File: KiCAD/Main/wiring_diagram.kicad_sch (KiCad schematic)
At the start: 19 parts, among them J5 Screw_Terminal_01x09, J6 Screw_Terminal_01x09, M1 Motor_Servo [Axon Mini MkII], M2 Motor_Servo [Axon Mini MkII], SW3 Screw Switch, SW4 Screw Switch, SW5 Screw Switch, SW6 Screw Switch

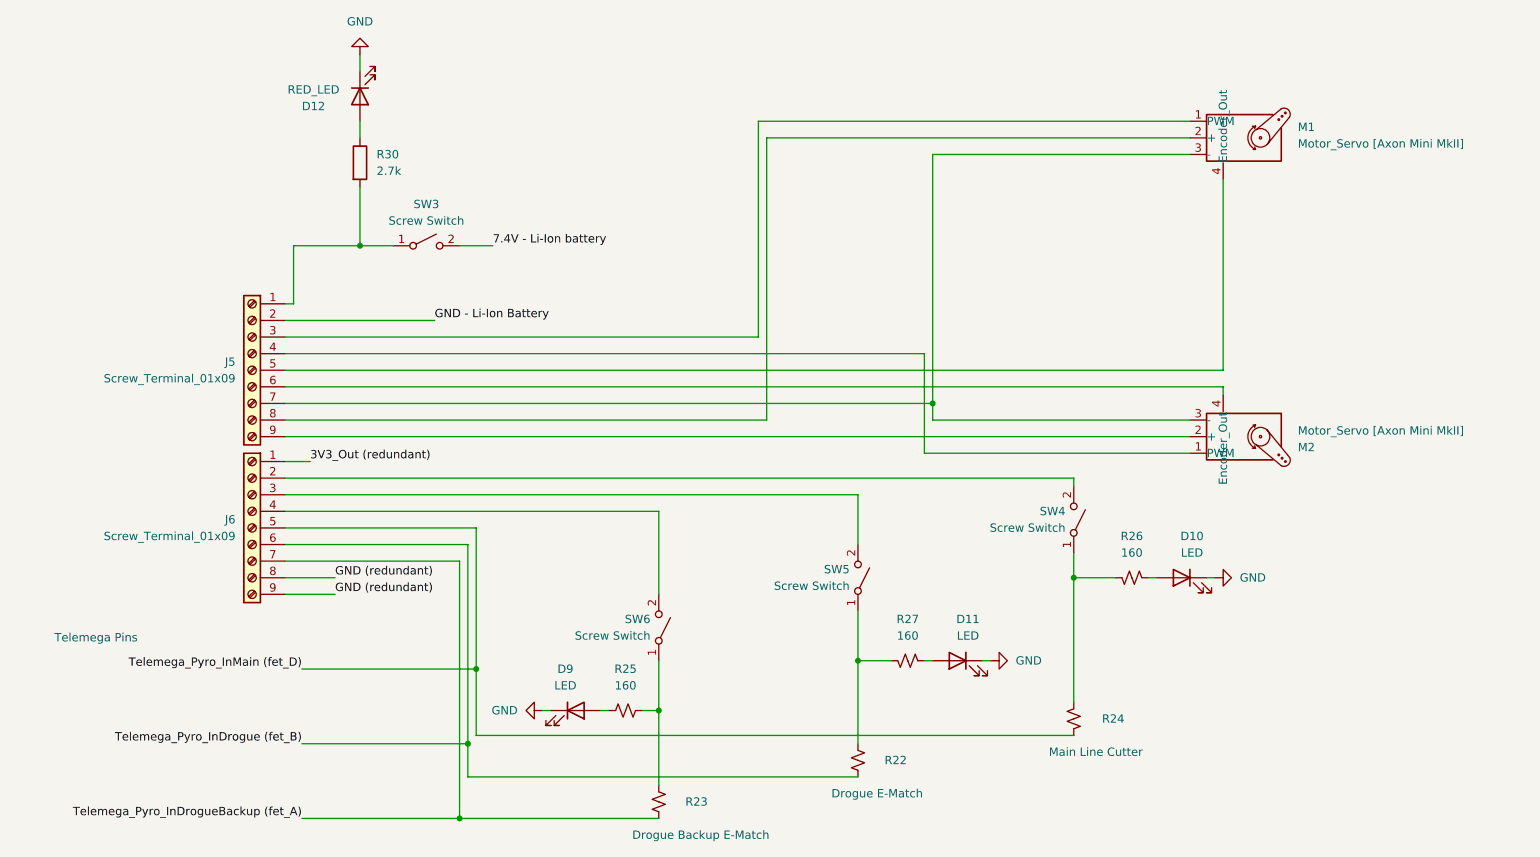
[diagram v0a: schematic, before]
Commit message: Marked components as ignored from board
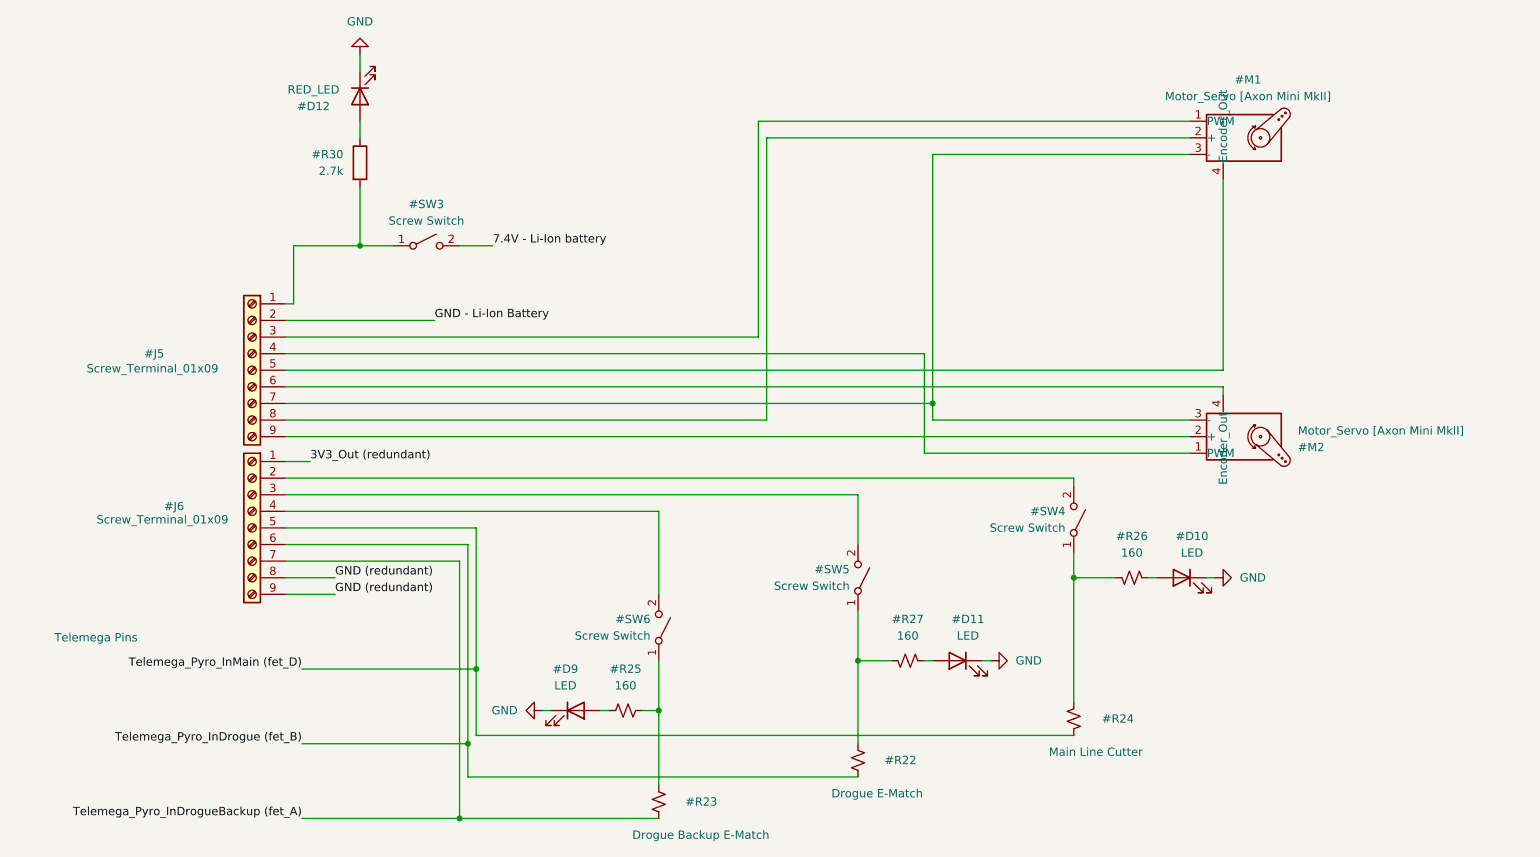
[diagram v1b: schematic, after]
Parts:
- renumbered D10 to #D10, D11 to #D11, D12 to #D12, D9 to #D9, J5 to #J5, J6 to #J6, M1 to #M1, M2 to #M2, R22 to #R22, R23 to #R23, R24 to #R24, R25 to #R25, R26 to #R26, R27 to #R27, R30 to #R30, SW3 to #SW3, SW4 to #SW4, SW5 to #SW5, SW6 to #SW6
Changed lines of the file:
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@@
 		(polyline
 			(pts
-				(xy 137.16 134.62) (xy 144.7799 134.62) (xy 144.7799 142.24) (xy 137.16 142.24)
+				(xy 57.15 120.65) (xy 57.15 148.59) (xy 17.78 148.59) (xy 17.78 121.92) (xy 17.78 120.65)
 			)
 			(stroke
@@
 		(polyline
 			(pts
-				(xy 57.15 120.65) (xy 57.15 148.59) (xy 17.78 148.59) (xy 17.78 121.92) (xy 17.78 120.65)
+				(xy 137.16 134.62) (xy 144.7799 134.62) (xy 144.7799 142.24) (xy 137.16 142.24)
 			)
 			(stroke
@@
 		(on_board yes)
 		(dnp no)
-		(property "Reference" "D12"
+		(property "Reference" "#D12"
 			(at 57.658 38.354 90)
 			(effects
@@
 			(project "Main"
 				(path "/bbb10697-a5dd-43b8-9c6f-4c5919cf3463/c1ec1855-540a-4992-9e52-86b4a82d5f82"
-					(reference "D12")
+					(reference "#D12")
 					(unit 1)
 				)
@@
 		(dnp no)
 		(fields_autoplaced yes)
-		(property "Reference" "D11"
+		(property "Reference" "#D11"
 			(at 157.7975 116.84 0)
 			(effects
@@
 			(project "Main"
 				(path "/bbb10697-a5dd-43b8-9c6f-4c5919cf3463/c1ec1855-540a-4992-9e52-86b4a82d5f82"
-					(reference "D11")
+					(reference "#D11")
 					(unit 1)
 				)
@@
 		(dnp no)
 		(fields_autoplaced yes)
-		(property "Reference" "M1"
-			(at 208.28 41.5404 0)
-			(effects
-				(font
-					(size 1.27 1.27)
-				)
-				(justify left)
+		(property "Reference" "#M1"
+			(at 200.6461 34.29 0)
+			(effects
+				(font
+					(size 1.27 1.27)
+				)
 			)
 		)
 		(property "Value" "Motor_Servo [Axon Mini MkII]"
-			(at 208.28 44.0804 0)
-			(effects
-				(font
-					(size 1.27 1.27)
-				)
-				(justify left)
+			(at 200.6461 36.83 0)
+			(effects
+				(font
+					(size 1.27 1.27)
+				)
 			)
 		)
@@
 			(project "Main"
 				(path "/bbb10697-a5dd-43b8-9c6f-4c5919cf3463/c1ec1855-540a-4992-9e52-86b4a82d5f82"
-					(reference "M1")
+					(reference "#M1")
 					(unit 1)
 				)
@@
 		(dnp no)
 		(fields_autoplaced yes)
-		(property "Reference" "D9"
+		(property "Reference" "#D9"
 			(at 96.2025 124.46 0)
 			(effects
@@
 			(project ""
 				(path "/bbb10697-a5dd-43b8-9c6f-4c5919cf3463/c1ec1855-540a-4992-9e52-86b4a82d5f82"
-					(reference "D9")
+					(reference "#D9")
 					(unit 1)
 				)
@@
 		(on_board yes)
 		(dnp no)
-		(property "Reference" "R22"
+		(property "Reference" "#R22"
 			(at 145.034 138.43 0)
 			(effects
@@
 			(project ""
 				(path "/bbb10697-a5dd-43b8-9c6f-4c5919cf3463/c1ec1855-540a-4992-9e52-86b4a82d5f82"
-					(reference "R22")
+					(reference "#R22")
 					(unit 1)
 				)
@@
 		(on_board yes)
 		(dnp no)
-		(property "Reference" "SW5"
+		(property "Reference" "#SW5"
 			(at 139.7 109.22 90)
 			(effects
@@
 			(project "Main"
 				(path "/bbb10697-a5dd-43b8-9c6f-4c5919cf3463/c1ec1855-540a-4992-9e52-86b4a82d5f82"
-					(reference "SW5")
+					(reference "#SW5")
 					(unit 1)
 				)
@@
 		(dnp no)
 		(fields_autoplaced yes)
-		(property "Reference" "SW3"
+		(property "Reference" "#SW3"
 			(at 74.93 53.34 0)
 			(effects
@@
 			(project ""
 				(path "/bbb10697-a5dd-43b8-9c6f-4c5919cf3463/c1ec1855-540a-4992-9e52-86b4a82d5f82"
-					(reference "SW3")
+					(reference "#SW3")
 					(unit 1)
 				)
@@
 		(dnp no)
 		(fields_autoplaced yes)
-		(property "Reference" "R26"
+		(property "Reference" "#R26"
 			(at 182.88 104.14 90)
 			(effects
@@
 			(project "Main"
 				(path "/bbb10697-a5dd-43b8-9c6f-4c5919cf3463/c1ec1855-540a-4992-9e52-86b4a82d5f82"
-					(reference "R26")
+					(reference "#R26")
 					(unit 1)
 				)
@@
 		(on_board yes)
 		(dnp no)
-		(fields_autoplaced yes)
-		(property "Reference" "J5"
-			(at 45.72 77.4699 0)
-			(effects
-				(font
-					(size 1.27 1.27)
-				)
-				(justify left)
+		(property "Reference" "#J5"
+			(at 33.274 76.2 0)
+			(effects
+				(font
+					(size 1.27 1.27)
+				)
 			)
 		)
 		(property "Value" "Screw_Terminal_01x09"
-			(at 45.72 80.0099 0)
-			(effects
-				(font
-					(size 1.27 1.27)
-				)
-				(justify left)
+			(at 33.02 78.486 0)
+			(effects
+				(font
+					(size 1.27 1.27)
+				)
 			)
 		)
@@
 			(project "Main"
 				(path "/bbb10697-a5dd-43b8-9c6f-4c5919cf3463/c1ec1855-540a-4992-9e52-86b4a82d5f82"
-					(reference "J5")
+					(reference "#J5")
 					(unit 1)
 				)
@@
 		(dnp no)
 		(fields_autoplaced yes)
-		(property "Reference" "R25"
+		(property "Reference" "#R25"
 			(at 105.41 124.46 90)
 			(effects
@@
 			(project ""
 				(path "/bbb10697-a5dd-43b8-9c6f-4c5919cf3463/c1ec1855-540a-4992-9e52-86b4a82d5f82"
-					(reference "R25")
+					(reference "#R25")
 					(unit 1)
 				)
@@
 		(on_board yes)
 		(dnp no)
-		(property "Reference" "R24"
+		(property "Reference" "#R24"
 			(at 178.308 132.08 0)
 			(effects
@@
 			(project "Main"
 				(path "/bbb10697-a5dd-43b8-9c6f-4c5919cf3463/c1ec1855-540a-4992-9e52-86b4a82d5f82"
-					(reference "R24")
+					(reference "#R24")
 					(unit 1)
 				)
@@
 		(on_board yes)
 		(dnp no)
-		(property "Reference" "SW4"
+		(property "Reference" "#SW4"
 			(at 172.72 100.33 90)
 			(effects
@@
 			(project "Main"
 				(path "/bbb10697-a5dd-43b8-9c6f-4c5919cf3463/c1ec1855-540a-4992-9e52-86b4a82d5f82"
-					(reference "SW4")
+					(reference "#SW4")
 					(unit 1)
 				)
@@
 		(on_board yes)
 		(dnp no)
-		(fields_autoplaced yes)
-		(property "Reference" "J6"
-			(at 45.72 101.5999 0)
-			(effects
-				(font
-					(size 1.27 1.27)
-				)
-				(justify left)
+		(property "Reference" "#J6"
+			(at 36.322 99.568 0)
+			(effects
+				(font
+					(size 1.27 1.27)
+				)
 			)
 		)
 		(property "Value" "Screw_Terminal_01x09"
-			(at 45.72 104.1399 0)
-			(effects
-				(font
-					(size 1.27 1.27)
-				)
-				(justify left)
+			(at 34.544 101.6 0)
+			(effects
+				(font
+					(size 1.27 1.27)
+				)
 			)
 		)
@@
 			(project "Main"
 				(path "/bbb10697-a5dd-43b8-9c6f-4c5919cf3463/c1ec1855-540a-4992-9e52-86b4a82d5f82"
-					(reference "J6")
+					(reference "#J6")
 					(unit 1)
 				)
@@
 		(dnp no)
 		(fields_autoplaced yes)
-		(property "Reference" "D10"
+		(property "Reference" "#D10"
 			(at 192.0875 104.14 0)
 			(effects
@@
 			(project "Main"
 				(path "/bbb10697-a5dd-43b8-9c6f-4c5919cf3463/c1ec1855-540a-4992-9e52-86b4a82d5f82"
-					(reference "D10")
+					(reference "#D10")
 					(unit 1)
 				)
@@
 		(on_board yes)
 		(dnp no)
-		(property "Reference" "SW6"
+		(property "Reference" "#SW6"
 			(at 109.22 116.84 90)
 			(effects
@@
 			(project "Main"
 				(path "/bbb10697-a5dd-43b8-9c6f-4c5919cf3463/c1ec1855-540a-4992-9e52-86b4a82d5f82"
-					(reference "SW6")
+					(reference "#SW6")
 					(unit 1)
 				)
@@
 		(on_board yes)
 		(dnp no)
-		(property "Reference" "R23"
+		(property "Reference" "#R23"
 			(at 114.554 144.78 0)
 			(effects
@@
 			(project "Main"
 				(path "/bbb10697-a5dd-43b8-9c6f-4c5919cf3463/c1ec1855-540a-4992-9e52-86b4a82d5f82"
-					(reference "R23")
+					(reference "#R23")
 					(unit 1)
 				)
@@
 		(dnp no)
 		(fields_autoplaced yes)
-		(property "Reference" "R27"
+		(property "Reference" "#R27"
 			(at 148.59 116.84 90)
 			(effects
@@
 			(project "Main"
 				(path "/bbb10697-a5dd-43b8-9c6f-4c5919cf3463/c1ec1855-540a-4992-9e52-86b4a82d5f82"
-					(reference "R27")
+					(reference "#R27")
 					(unit 1)
 				)
@@
 		(dnp no)
 		(fields_autoplaced yes)
-		(property "Reference" "R30"
-			(at 67.31 45.72 0)
-			(effects
-				(font
-					(size 1.27 1.27)
-				)
-				(justify left)
+		(property "Reference" "#R30"
+			(at 62.23 45.7199 0)
+			(effects
+				(font
+					(size 1.27 1.27)
+				)
+				(justify right)
 			)
 		)
 		(property "Value" "2.7k"
-			(at 67.31 48.26 0)
-			(effects
-				(font
-					(size 1.27 1.27)
-				)
-				(justify left)
+			(at 62.23 48.2599 0)
+			(effects
+				(font
+					(size 1.27 1.27)
+				)
+				(justify right)
 			)
 		)
@@
 			(project ""
 				(path "/bbb10697-a5dd-43b8-9c6f-4c5919cf3463/c1ec1855-540a-4992-9e52-86b4a82d5f82"
-					(reference "R30")
+					(reference "#R30")
 					(unit 1)
 				)
@@
 		(on_board yes)
 		(dnp no)
-		(property "Reference" "M2"
+		(property "Reference" "#M2"
 			(at 208.28 90.5396 0)
 			(effects
@@
 			(project "Main"
 				(path "/bbb10697-a5dd-43b8-9c6f-4c5919cf3463/c1ec1855-540a-4992-9e52-86b4a82d5f82"
-					(reference "M2")
-					(unit 1)
-				)
+					(reference "#M2")
+					(unit 1)
+				)
